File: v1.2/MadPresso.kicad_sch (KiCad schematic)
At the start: 42 parts, among them J1 Conn_01x07, J2 Conn_01x03, J3 Conn_01x02, J4 Conn_01x04, Q1 BC847, Q2 BSS84, U1 LTV-356T, U2 ADC101C021CIMK, U3 WeMos_D1_mini

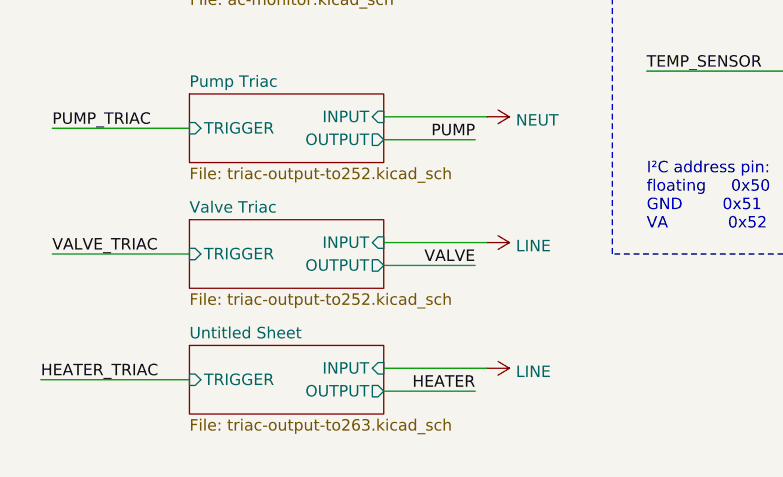
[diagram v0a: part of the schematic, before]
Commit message: Revert Q7 back to DPAK
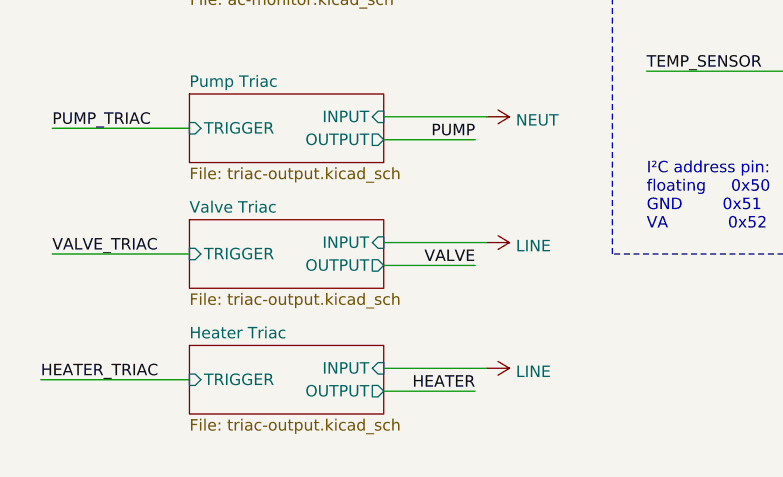
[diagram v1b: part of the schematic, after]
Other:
- removed sheet Untitled Sheet
- added sheet Heater Triac (triac-output.kicad_sch)
- sheet Pump Triac: file triac-output-to252.kicad_sch -> triac-output.kicad_sch
- sheet Valve Triac: file triac-output-to252.kicad_sch -> triac-output.kicad_sch

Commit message: change q7 to TO263 (D2PAK) package
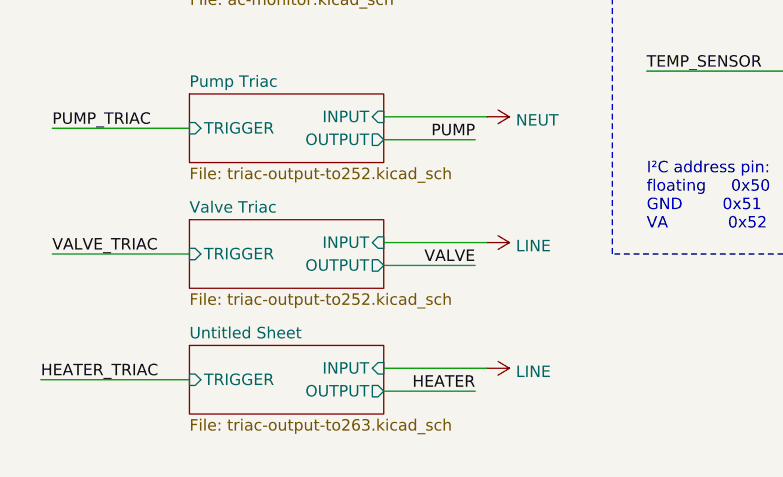
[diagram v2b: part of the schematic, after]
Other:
- removed sheet Heater Triac
- added sheet Untitled Sheet (triac-output-to263.kicad_sch)
- sheet Pump Triac: file triac-output.kicad_sch -> triac-output-to252.kicad_sch
- sheet Valve Triac: file triac-output.kicad_sch -> triac-output-to252.kicad_sch
